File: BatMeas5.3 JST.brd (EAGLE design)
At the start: 70 x 35 mm, 50 parts, among them IC1 ATTINY24, IC2 3V3, IC3 3V, J4 BM05B-PASS-1-TFT_(LF)(SN)SMD, T1 MMUN2233, T2 MMUN2233, T3 MMUN2233, T4 MMUN2111LT1G, T5 MMUN2111LT1G, T6 MMUN2111LT1G, T7 MMUN2233, T8 MMUN2233

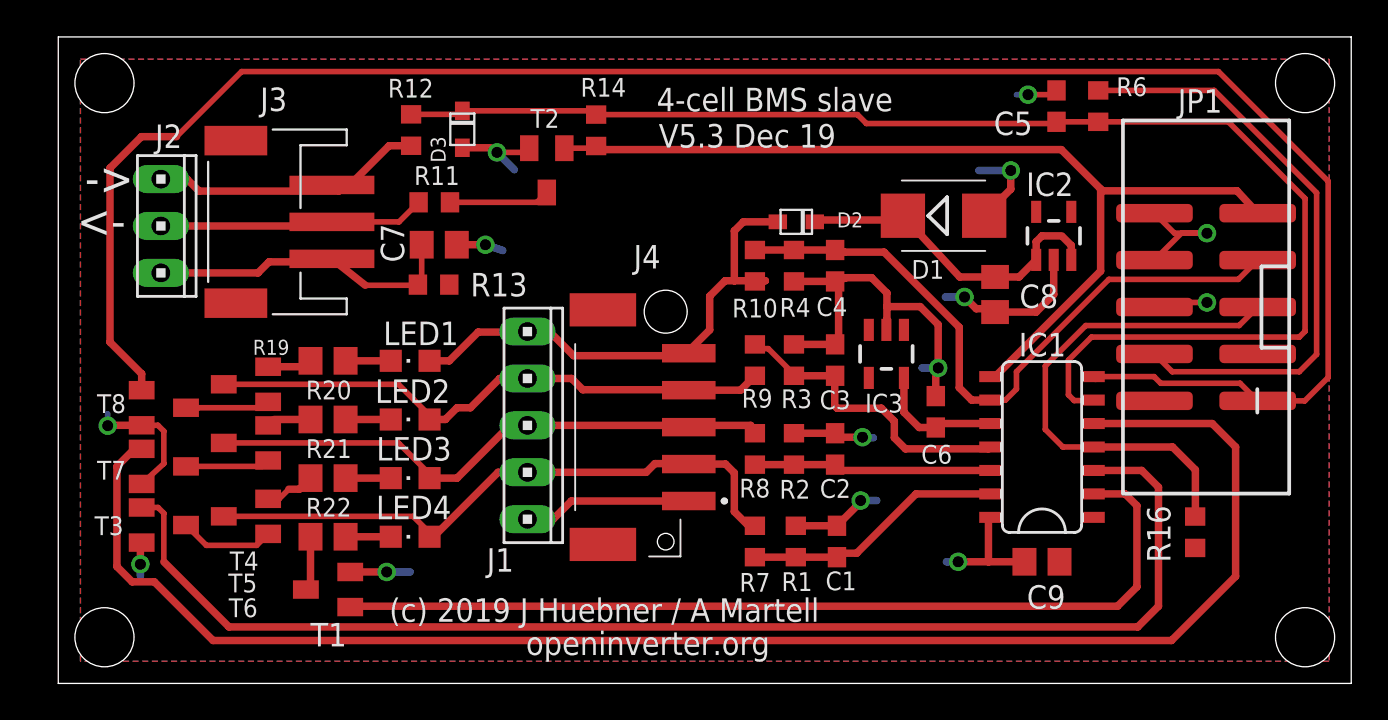
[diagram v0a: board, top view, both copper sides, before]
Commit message: Replaced JST comms connector by AVX or 4mm IDC wire to board connector Removed all THT options Removed holes below cell JST connector, made pads longer
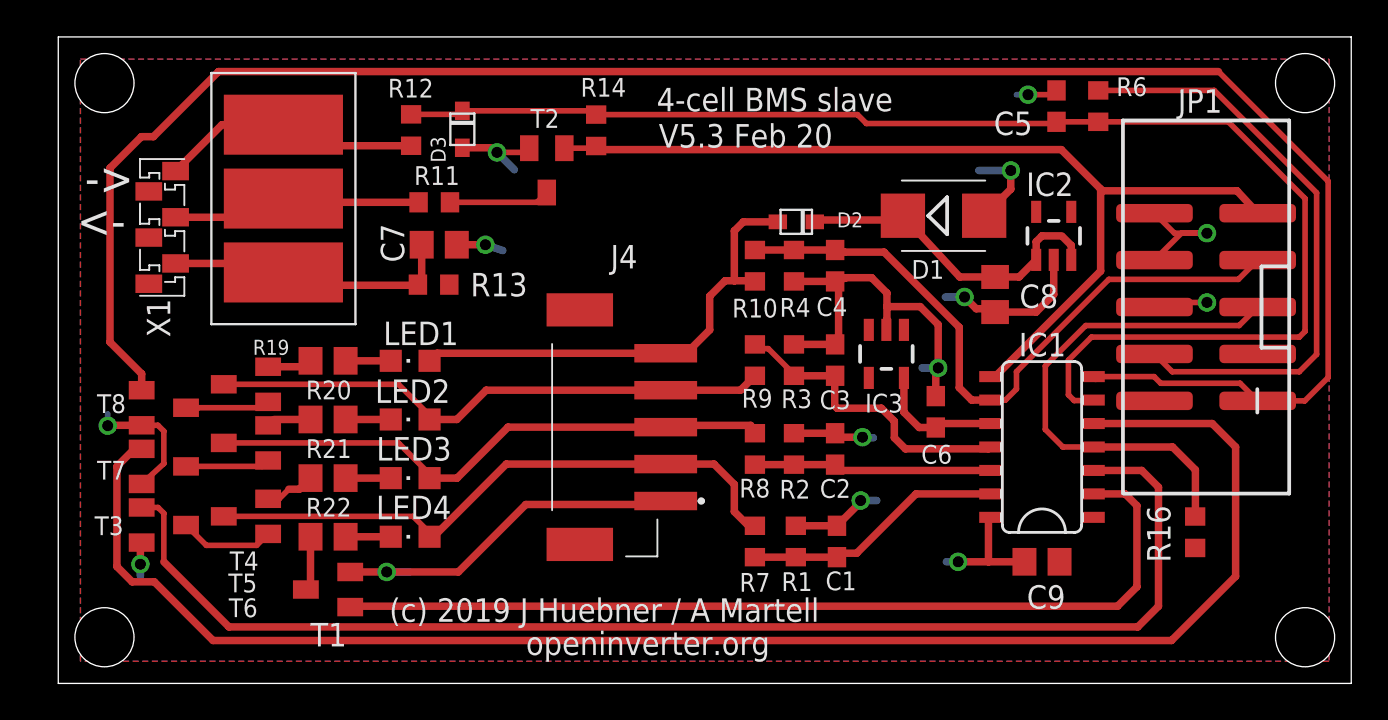
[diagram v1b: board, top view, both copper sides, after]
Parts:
- removed J1: (no value), con-amp:10X05MTA
- removed J2: (no value), con-amp:10X03MTA
- removed J3: (no value), adafruit:JSTPH3
- added X1: 009175003, con-avx:009175003
- added X1_: 4400W03J7923, con-avx:4400WXXJ7923
- moved J4 1.25 mm to (29.8, 11.9)
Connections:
- net GND: no longer J1.1
- net N$12: now also X1.1@1, X1_.P$1; no longer J2.1, J3.1
- net N$17: no longer J1.5
- net N$22: now also X1.3@2, X1_.P$3; no longer J2.3, J3.3
- net N$23: no longer J1.4
- net N$24: no longer J1.3
- net N$25: no longer J1.2
- net TX: now also X1.2@1, X1_.P$2; no longer J2.2, J3.2
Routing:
- net GND: track 93.3 -> 102.9 mm
- net TX: track 14.8 -> 16.9 mm
- net N$17: track 28.1 -> 26.1 mm
- net N$24: track 31.3 -> 32.3 mm
- net N$12: track 17.4 -> 16.6 mm
- net N$25: track 33.6 -> 34.4 mm
- net N$23: track 31.2 -> 31.9 mm
- net N$22: track 15.6 -> 14.9 mm
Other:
- board text added: "V5.3 Feb 20"
- board text removed: "V5.3 Dec 19"

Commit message: Updated BOM
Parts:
- C5: value 4n7 -> 10n
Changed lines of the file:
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@@
 <attribute name="VALUE" x="20.9925" y="27.9525" size="1.27" layer="27" rot="R180"/>
 </element>
-<element name="C5" library="rcl" package="C0603" value="4n7" x="54.0425" y="31.255" smashed="yes" rot="R90">
+<element name="C5" library="rcl" package="C0603" value="10n" x="54.0425" y="31.255" smashed="yes" rot="R90">
 <attribute name="NAME" x="52.7425" y="30.9575" size="1.27" layer="25" rot="R180"/>
 <attribute name="VALUE" x="55.9475" y="30.62" size="1.27" layer="27" rot="R90"/>
